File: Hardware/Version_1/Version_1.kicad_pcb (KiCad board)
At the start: 6 copper layers, 65 x 30 mm, 94 parts, among them IC1 W25R256JVEIQ, IC3 TPS62A01DRLR, IC4 TPS62A01DRLR, IC5 TPS62A01DRLR, IC6 LIFCL-40-7BG256C, IC7 IS46TR16128D-125KBLA2, J1 GPIO, J2 52435-2271, J3 Conn_01x05_Pin, J4 52435-2271, U1 CAT24C256

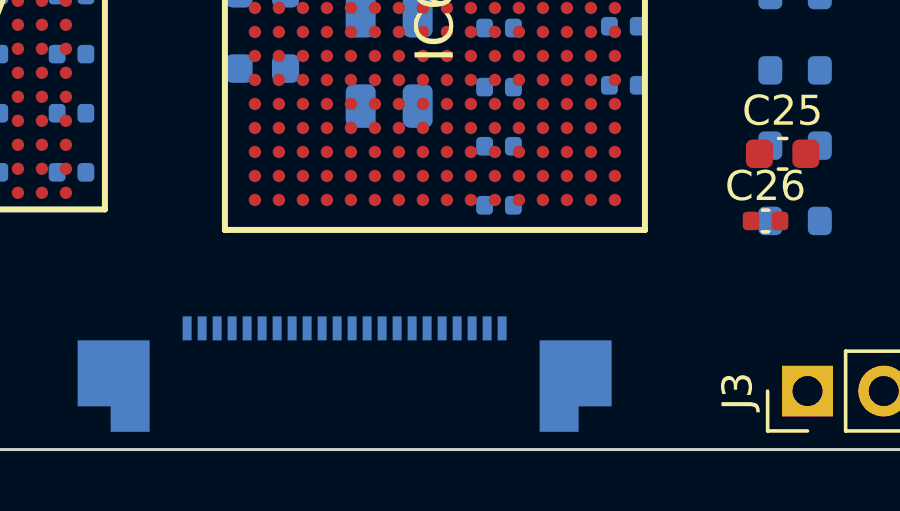
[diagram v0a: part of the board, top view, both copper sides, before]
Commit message: added pll
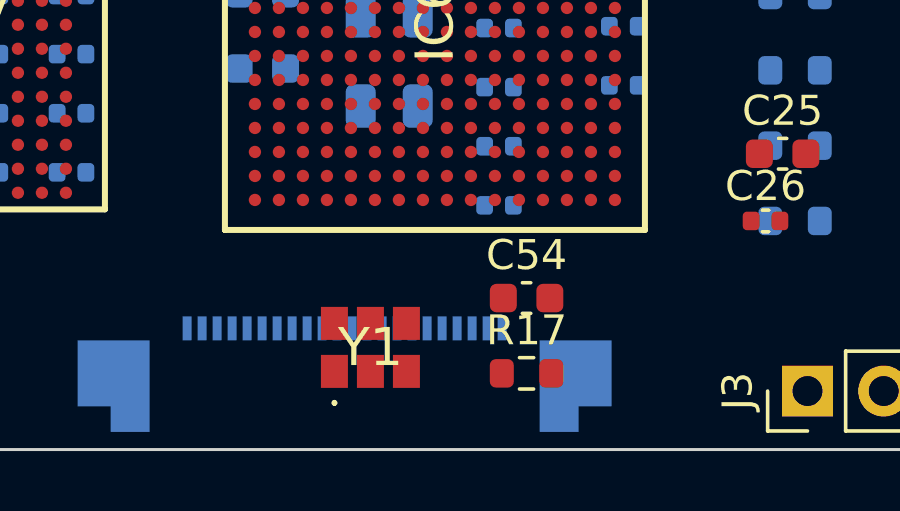
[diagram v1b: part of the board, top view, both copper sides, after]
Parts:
- added C54: 100n, Capacitor_SMD:C_0603_1608Metric, F.Cu at (137.3, 95.0)
- added R17: 100, Resistor_SMD:R_0603_1608Metric, F.Cu at (137.3, 97.5)
- added Y1: AK3ADDF1-156.2500T3, Component:AK3ADDF11562500T3, F.Cu at (132.1, 96.6)
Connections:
- IC6 pad G7: unconnected-(IC6-VCCAUX_2-PadG7) -> /VCCAUX

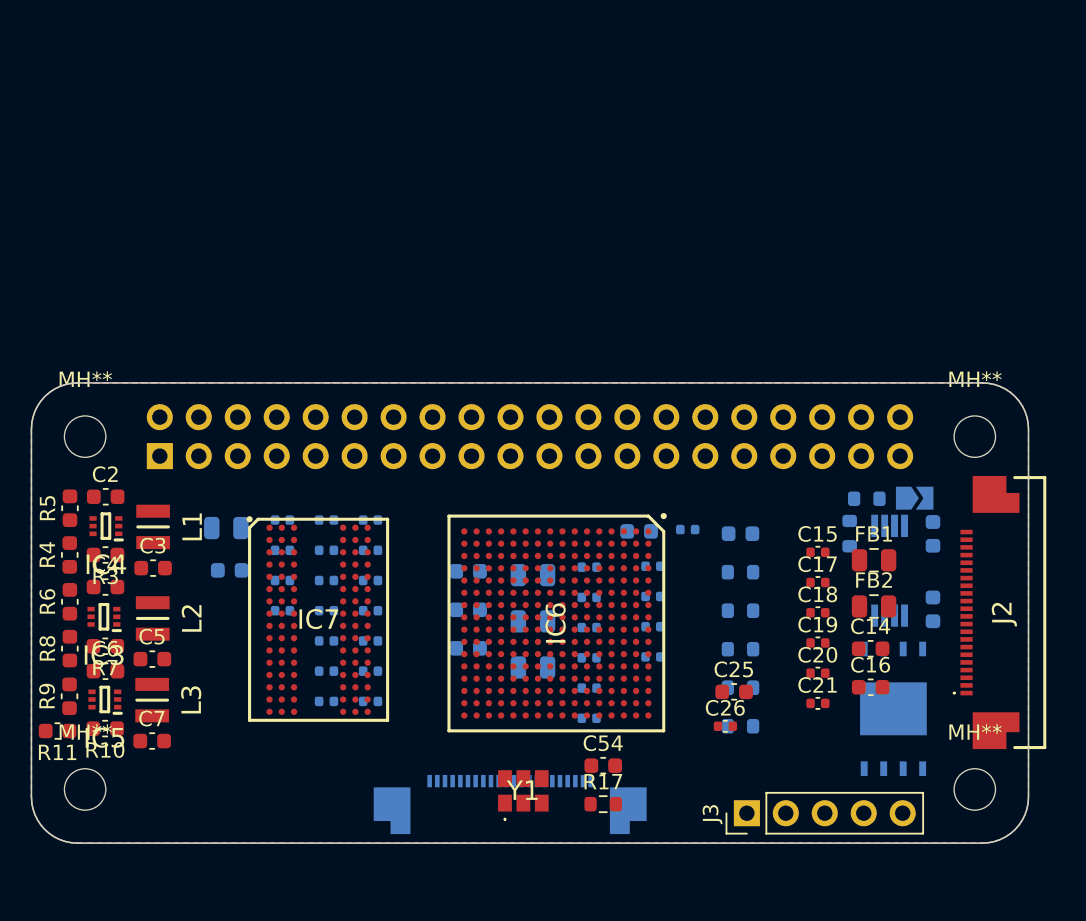
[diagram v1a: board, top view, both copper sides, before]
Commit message: Done routing for first DQS group
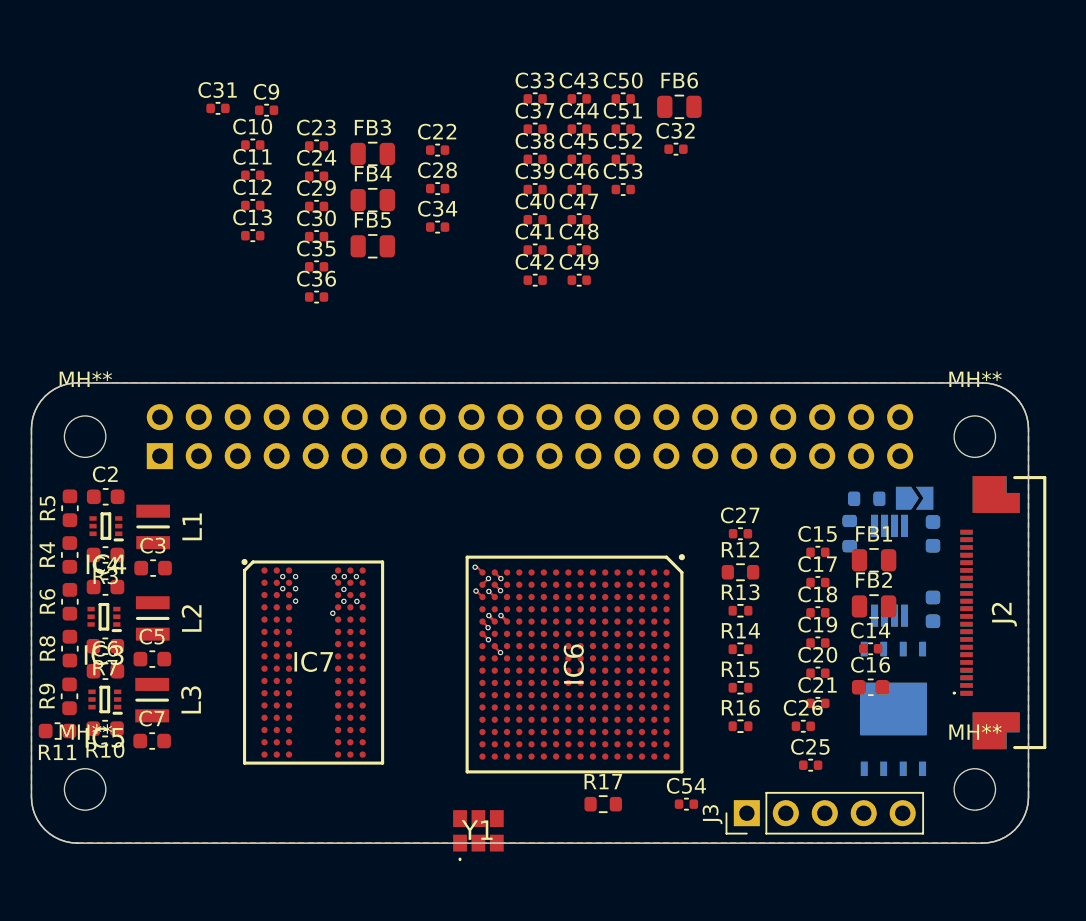
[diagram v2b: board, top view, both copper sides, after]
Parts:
- C10, C11, C12, C13, C23, C24, C29, C30, C31, C33, C35, C36, C37, C38, C39, C40, C41, C42, C43, C44, C45, C46, C47, C48, C49, C50, C51, C52, C53, FB3, FB4, FB5, FB6, R12: moved to F.Cu
- C14, C25, C54: footprint Capacitor_SMD:C_0603_1608Metric -> Capacitor_SMD:C_0402_1005Metric
- C22, C27, C28, C32, C34, C9: footprint Capacitor_SMD:C_0603_1608Metric -> Capacitor_SMD:C_0402_1005Metric; moved to F.Cu
- R13, R14, R15, R16: footprint Resistor_SMD:R_0603_1608Metric -> Resistor_SMD:R_0402_1005Metric; moved to F.Cu
- moved C31 41.1 mm to (112.2, 52.1), turned to 0 degrees
- moved FB6 40.3 mm to (142.2, 52.0), turned to 0 degrees
- moved C32 40.0 mm to (142.0, 54.8), turned to 0 degrees
- moved C10 37.9 mm to (114.4, 54.5), turned to 0 degrees
- moved C11 37.9 mm to (114.4, 56.5), turned to 0 degrees
- moved C12 37.9 mm to (114.4, 58.4), turned to 0 degrees
- moved C13 37.9 mm to (114.4, 60.4), turned to 0 degrees
- moved C9 36.7 mm to (115.3, 52.2), turned to 0 degrees
- moved C50 35.3 mm to (138.6, 51.5), turned to 0 degrees
- moved C51 35.3 mm to (138.6, 53.5), turned to 0 degrees
- moved C52 35.3 mm to (138.6, 55.4), turned to 0 degrees
- moved C53 35.3 mm to (138.6, 57.4), turned to 0 degrees
- moved J4 35.0 mm to (163.5, 85.0), turned to -90 degrees
- moved C23 32.7 mm to (118.6, 54.5), turned to 0 degrees
- moved C24 32.7 mm to (118.6, 56.5), turned to 0 degrees
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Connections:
- IC6 pad M8: /DQSU# -> /DQSL#
- IC6 pad M9: /DQSU -> /DQSL
- IC6 pad P5: /DQSL# -> /DQSU-
- IC6 pad P6: /DQU4 -> /DQL4
- IC6 pad P7: /DQU5 -> /DQL5
- IC6 pad P8: /DQU6 -> /DQL6
- IC6 pad P9: /DQU7 -> /DQL7
- IC6 pad R1: /DQL0 -> /DQU3
- IC6 pad R2: /DQL1 -> /DQU5
- IC6 pad R3: /DQL2 -> /DQU4
- IC6 pad R4: /DQL5 -> unconnected-(IC6-PB24A-PadR4)
- IC6 pad R5: /DQSL -> /DQSU+
- IC6 pad R7: unconnected-(IC6-PB28B-PadR7) -> /DQU6
- IC6 pad R8: /DQU2 -> /DQL2
- IC6 pad R9: /DQU3 -> /DQL3
- IC6 pad T10: /DQU1 -> /DQL1
- IC6 pad T2: /DQL3 -> /DQU7
- IC6 pad T3: /DQL4 -> /DQU1
- IC6 pad T4: /DQL6 -> unconnected-(IC6-PB20B-PadT4)
- IC6 pad T5: /DQL7 -> /DQU2
- IC6 pad T6: unconnected-(IC6-PB28A-PadT6) -> /DQU0
- IC6 pad T9: /DQU0 -> /DQL0
- IC7 pad B7: /DQSU# -> /DQSU-
- IC7 pad C7: /DQSU -> /DQSU+
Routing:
- net /DQU3: track 0.00 -> 21.8 mm, vias 0 -> 2
- net /DQU5: track 0.00 -> 21.8 mm, vias 0 -> 2
- net /DQU1: track 0.00 -> 21.8 mm, vias 0 -> 2
- net /DQU7: track 0.00 -> 21.7 mm, vias 0 -> 2
- net /DQU6: track 0.00 -> 21.7 mm, vias 0 -> 2
- net /DQU2: track 0.00 -> 21.7 mm, vias 0 -> 2
- net /DQSU-: track 0.00 -> 21.6 mm, vias 0 -> 2
- net /DQU0: track 0.00 -> 21.6 mm, vias 0 -> 2
- net /DQSU+: track 0.00 -> 21.6 mm, vias 0 -> 2
- net /DQU4: track 0.00 -> 21.6 mm, vias 0 -> 2
- net GND: track 0.00 -> 0.62 mm, vias 0 -> 3
- added copper zone on In2.Cu, net GND

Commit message: DRAM DQ groups
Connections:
- net /DQSL renamed /DQSL_P
- net /DQSL# renamed /DQSL_N
- net /DQSU+ renamed /DQSU_P
- net /DQSU- renamed /DQSU_N
- IC6 pad P6: /DQL4 -> /DQL1
- IC6 pad P7: /DQL5 -> /DQL3
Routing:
- net /DQL6: track 0.00 -> 19.9 mm, vias 0 -> 2
- net /DQL2: track 0.00 -> 19.9 mm, vias 0 -> 2
- net /DQL4: track 0.00 -> 19.9 mm, vias 0 -> 2
- net /DQSL_P: track 0.00 -> 19.9 mm, vias 0 -> 2
- net /DQL0: track 0.00 -> 19.9 mm, vias 0 -> 2
- net /DQL7: track 0.00 -> 19.9 mm, vias 0 -> 2
- net /DQSL_N: track 0.00 -> 19.8 mm, vias 0 -> 2
- net /DQL5: track 0.00 -> 19.8 mm, vias 0 -> 2
- net /DQL3: track 0.00 -> 19.8 mm, vias 0 -> 2
- net /DQSU_P: track 21.6 -> 18.9 mm
- net /DQU3: track 21.8 -> 19.8 mm
- net /DQU5: track 21.8 -> 19.8 mm
- net /DQU2: track 21.7 -> 19.7 mm
- net /DQU7: track 21.7 -> 19.8 mm
- net /DQU1: track 21.8 -> 19.8 mm
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
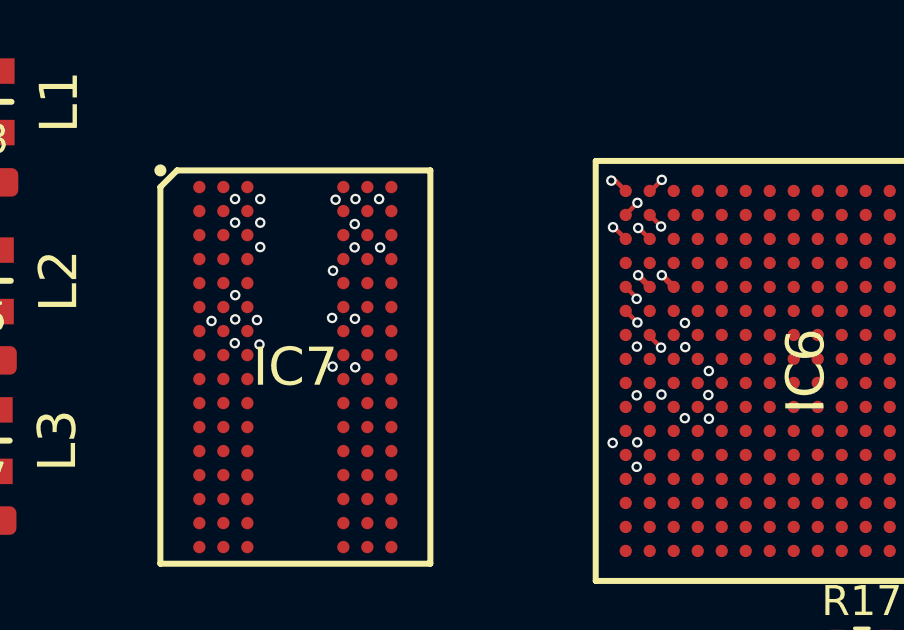
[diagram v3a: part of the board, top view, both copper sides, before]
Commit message: Redid routing with custom meadering paramters
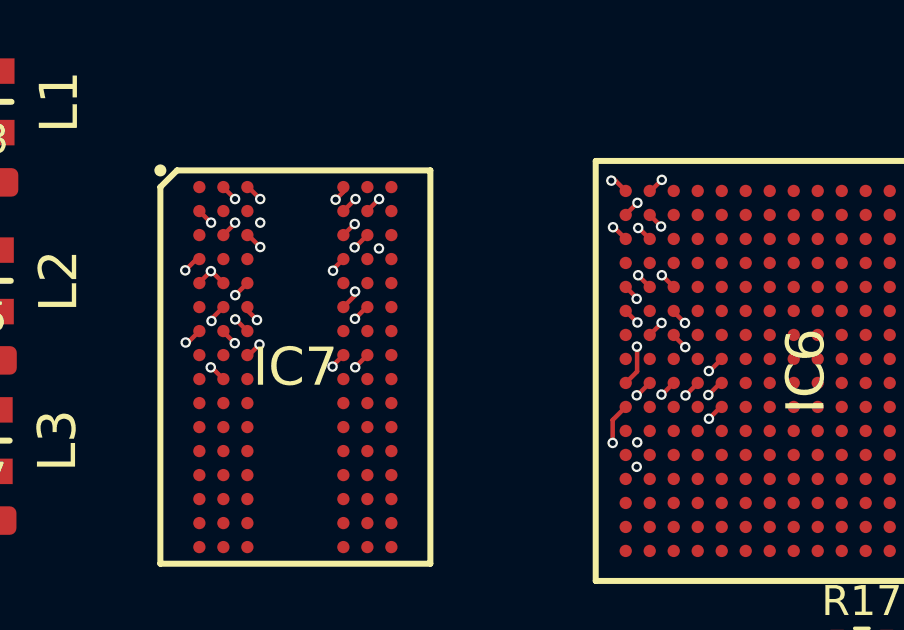
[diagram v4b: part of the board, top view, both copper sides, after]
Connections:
- IC6 pad M10: unconnected-(IC6-PB46A-PadM10) -> /DQL6
- IC6 pad N9: unconnected-(IC6-PB36B-PadN9) -> /DQL4
- IC6 pad R9: /DQL3 -> /DQL5
- IC6 pad T10: /DQL1 -> /DQL2
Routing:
- net /DQL1: track 0.00 -> 19.4 mm
- net GND: track 0.62 -> 4.13 mm, vias 3 -> 8
- net /DQSU_P: track 18.9 -> 19.6 mm

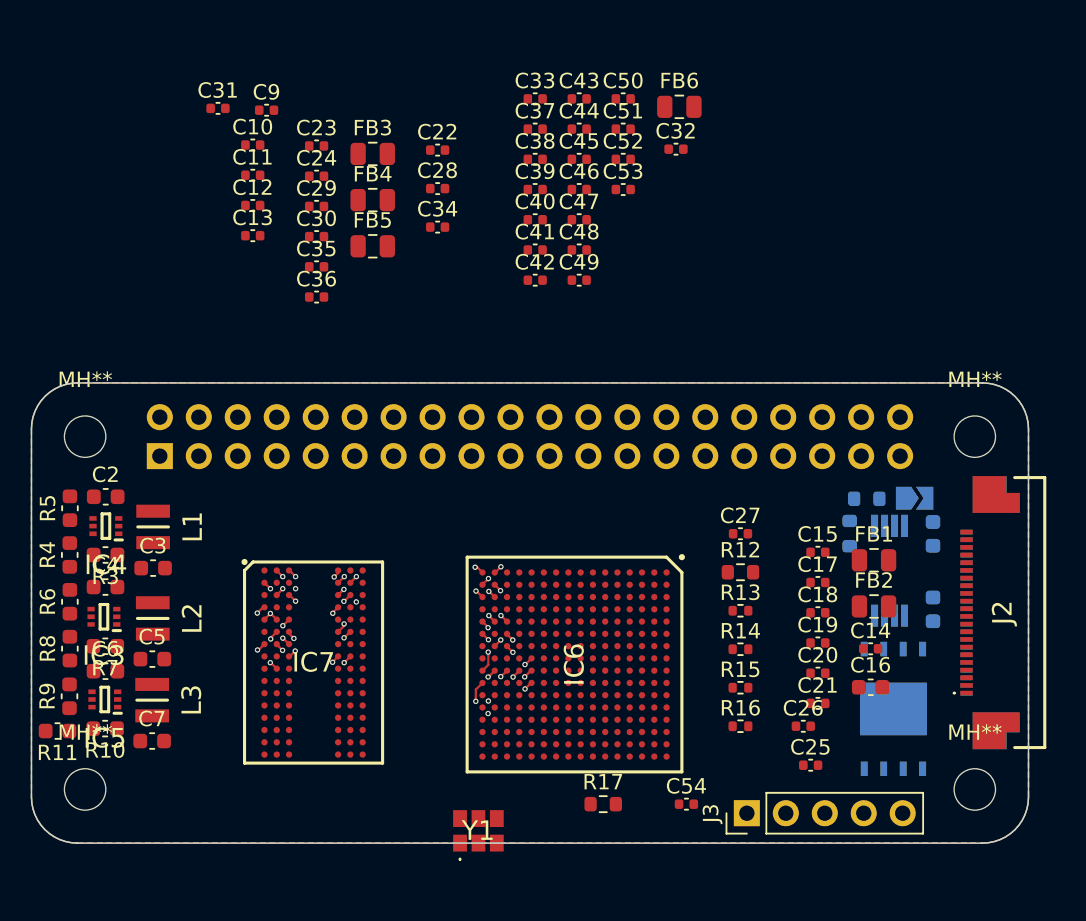
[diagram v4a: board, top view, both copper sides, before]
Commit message: Started routing DDR address lines
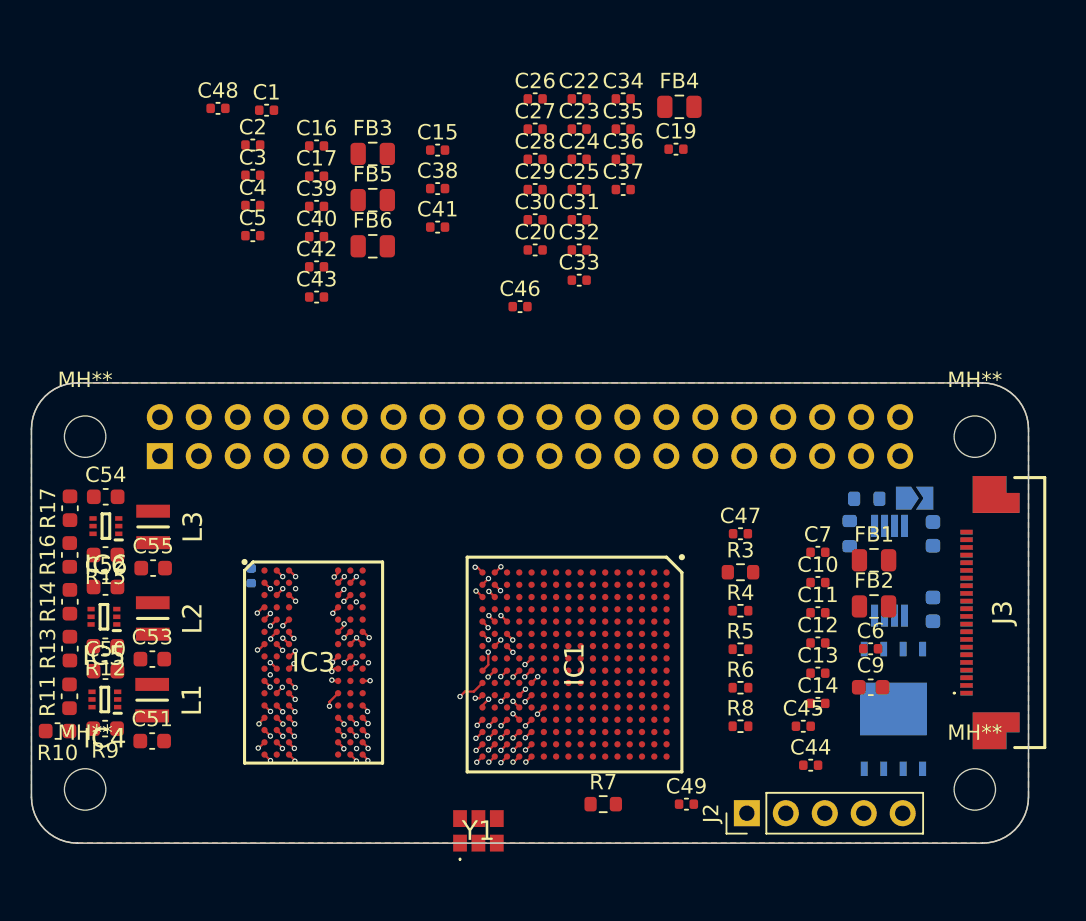
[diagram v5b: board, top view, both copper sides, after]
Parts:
- added C46: 100n, Capacitor_SMD:C_0402_1005Metric, F.Cu at (131.9, 65.0)
- C21: renamed from C42; moved to B.Cu
- moved C21 26.7 mm to (114.3, 82.6), turned to -90 degrees
- renumbered C9 to C1, C17 to C10, C18 to C11, C19 to C12, C20 to C13, C21 to C14, C22 to C15, C23 to C16, C24 to C17, C8 to C18, C32 to C19, C10 to C2, C41 to C20, C43 to C22, C44 to C23, C45 to C24, C46 to C25, C33 to C26, C37 to C27, C38 to C28, C39 to C29, C11 to C3, C40 to C30, C47 to C31, C48 to C32, C49 to C33, C50 to C34, C51 to C35, C52 to C36, C53 to C37, C28 to C38, C29 to C39, C12 to C4, C30 to C40, C34 to C41, C35 to C42, C36 to C43, C25 to C44, C26 to C45, C27 to C47, C31 to C48, C54 to C49, C13 to C5, C6 to C50, C7 to C51, C4 to C52, C5 to C53, C2 to C54, C3 to C55, C14 to C6, C15 to C7, C1 to C8, C16 to C9, FB6 to FB4, FB4 to FB5, FB5 to FB6, IC6 to IC1, IC1 to IC2, IC7 to IC3, IC5 to IC4, IC3 to IC5, IC4 to IC6, J3 to J2, J2 to J3, L3 to L1, L1 to L3, R11 to R10, R9 to R11, R7 to R12, R8 to R13, R6 to R14, R3 to R15, R4 to R16, R5 to R17, R12 to R3, R13 to R4, R14 to R5, R15 to R6, R17 to R7, R16 to R8, R10 to R9
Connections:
- IC1 pad L11: /A5 -> unconnected-(IC1-PB80A-PadL11)
- IC1 pad L12: /A4 -> /WE#
- IC1 pad M11: /A11 -> /CKE
- IC1 pad M12: /BA2 -> unconnected-(IC1-PB78A-PadM12)
- IC1 pad M13: unconnected-(IC6-PB82A-PadM13) -> /A10
- IC1 pad M14: /A6 -> /BA1
- IC1 pad M15: unconnected-(IC6-PB84B-PadM15) -> /A1
- IC1 pad M16: /A8 -> /A9
- IC1 pad N11: /A1 -> /RAS#
- IC1 pad N12: /ODT -> /CAS#
- IC1 pad N13: /A7 -> /ODT
- IC1 pad N14: /RAS# -> /A12
- IC1 pad N15: unconnected-(IC6-PB76B-PadN15) -> /A2
- IC1 pad N16: /A9 -> /A7
- IC1 pad P12: unconnected-(IC6-VCCIO3-PadP12) -> +1V0
- IC1 pad P15: unconnected-(IC6-PB72A-PadP15) -> /A5
- IC1 pad P16: unconnected-(IC6-PB72B-PadP16) -> /A8
- IC1 pad P8: /DQL6 -> unconnected-(IC1-PB42B-PadP8)
- IC1 pad R10: /BA1 -> unconnected-(IC1-PB56B-PadR10)
- IC1 pad R12: /A3 -> unconnected-(IC1-PB60A-PadR12)
- IC1 pad R13: /BA0 -> /BA2
- IC1 pad R14: /WE# -> /A3
- IC1 pad R15: /A12 -> /A6
- IC1 pad R16: /A10 -> /A13
- IC1 pad R8: /DQL2 -> unconnected-(IC1-PB42A-PadR8)
- IC1 pad T11: /CLK# -> /CLK_N
- IC1 pad T12: /CLK -> /CLK_P
- IC1 pad T13: unconnected-(IC6-PB60B-PadT13) -> /BA0
- IC1 pad T14: /CKE -> /A4
- IC1 pad T15: /CAS# -> /A11
- IC3 pad J7: /CK -> /CLK_P
- IC3 pad K7: /CK# -> /CLK_N
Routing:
- net /ODT: track 0.00 -> 17.8 mm, vias 0 -> 2
- net /WE#: track 0.00 -> 17.8 mm, vias 0 -> 2
- net /RAS#: track 0.00 -> 17.2 mm, vias 0 -> 2
- net /CS#: track 0.00 -> 16.4 mm, vias 0 -> 2
- net /CAS#: track 0.00 -> 16.3 mm, vias 0 -> 2
- net /CKE: track 0.00 -> 12.4 mm, vias 0 -> 2
- net /CLK_P: track 0.00 -> 12.2 mm, vias 0 -> 2
- net /CLK_N: track 0.00 -> 11.1 mm, vias 0 -> 2
- net /DQL7: track 19.6 -> 13.0 mm
- net GND: track 4.13 -> 10.8 mm, vias 8 -> 20
- net /DQL4: track 19.7 -> 17.1 mm
- net /DQL2: track 19.7 -> 17.2 mm
- net /VCCDRAM: track 0.00 -> 2.18 mm, vias 0 -> 6
- net /A10: track 0.00 -> 1.64 mm, vias 0 -> 2
- net /A11: track 0.00 -> 1.16 mm, vias 0 -> 2
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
